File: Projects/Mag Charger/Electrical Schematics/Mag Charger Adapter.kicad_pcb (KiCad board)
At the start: 2 copper layers, 26 x 13.4 mm, 4 parts, among them J1 Conn_01x08, J3 DX07S016JA3R1500

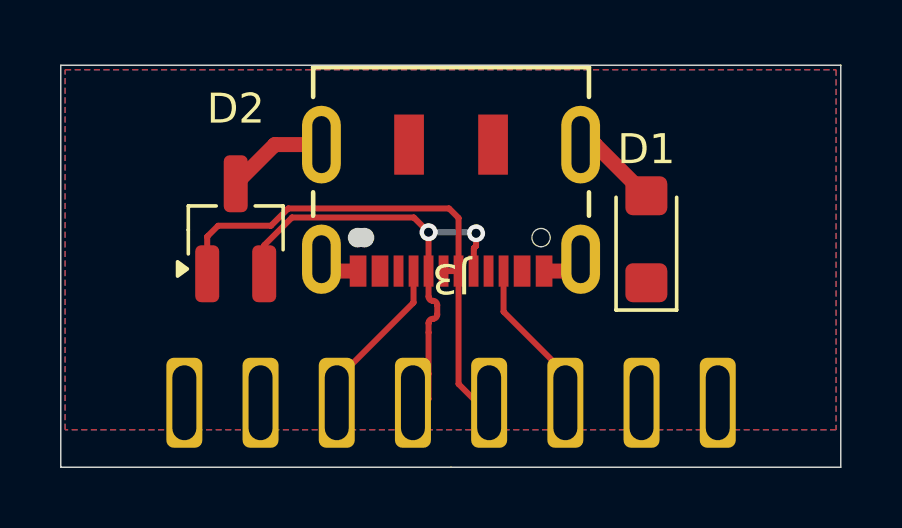
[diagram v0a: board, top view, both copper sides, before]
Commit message: Updated diode models
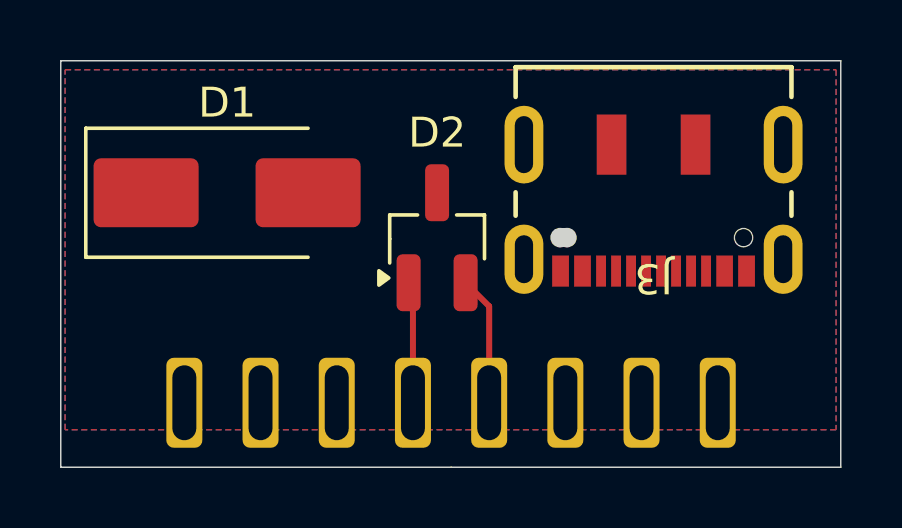
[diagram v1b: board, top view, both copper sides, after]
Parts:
- D1: footprint Diode_SMD:D_SMF -> Diode_SMD:D_SMB_Handsoldering
- moved D1 14.1 mm to (147.0, 138.0), turned to 0 degrees
- moved J3 6.75 mm to (161.2, 137.4)
- moved D2 6.72 mm to (154.0, 139.5)
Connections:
- D2 pad 1: /USB_DP -> /USB_DN
- D2 pad 2: /USB_DN -> /USB_DP
- J3 pad : GND -> (no net)
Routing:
- net /USB_DP: track 17.6 -> 4.33 mm
- net /USB_DN: track 16.5 -> 4.06 mm, vias 2 -> 0
- net GND: track 9.06 -> 0.00 mm
- net /USB_VCONN: track 5.84 -> 0.00 mm
- net /USB_CC: track 5.64 -> 0.00 mm
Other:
- board size 26 x 13.4 mm -> 26 x 13.6 mm

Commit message: Fixed adapter PCB
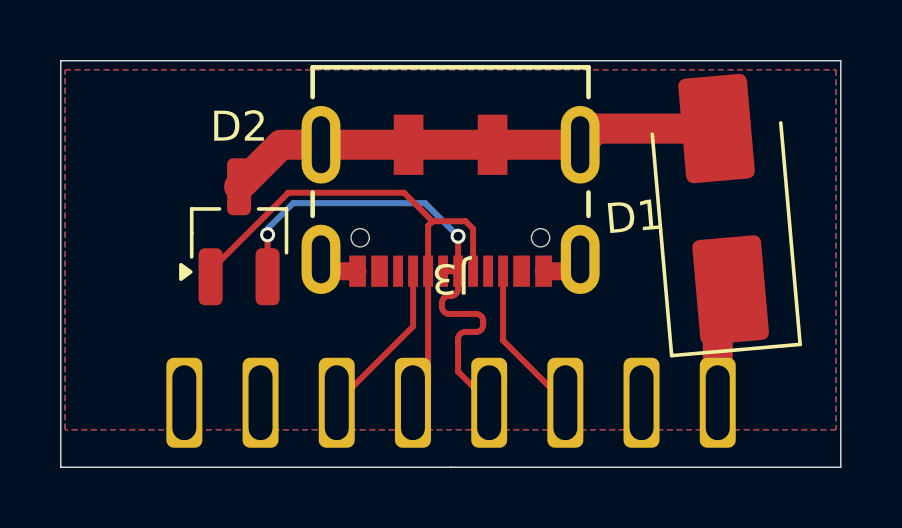
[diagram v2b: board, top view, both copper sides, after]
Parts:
- moved D1 16.6 mm to (163.6, 138.6), turned to 95 degrees
- moved J3 6.77 mm to (154.4, 137.4)
- moved D2 6.60 mm to (147.4, 139.3)
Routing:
- net GND: track 0.00 -> 19.5 mm
- net /USB_DN: track 4.06 -> 18.3 mm
- net /USB_DP: track 4.33 -> 17.4 mm, vias 0 -> 2
- net /USB_VCONN: track 0.00 -> 5.44 mm
- net /USB_CC: track 0.00 -> 5.24 mm
- net VBUS: track 0.00 -> 3.94 mm
